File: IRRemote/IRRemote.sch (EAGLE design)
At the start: 18 parts, among them U1 PNA460XM, U3 ATTINY841

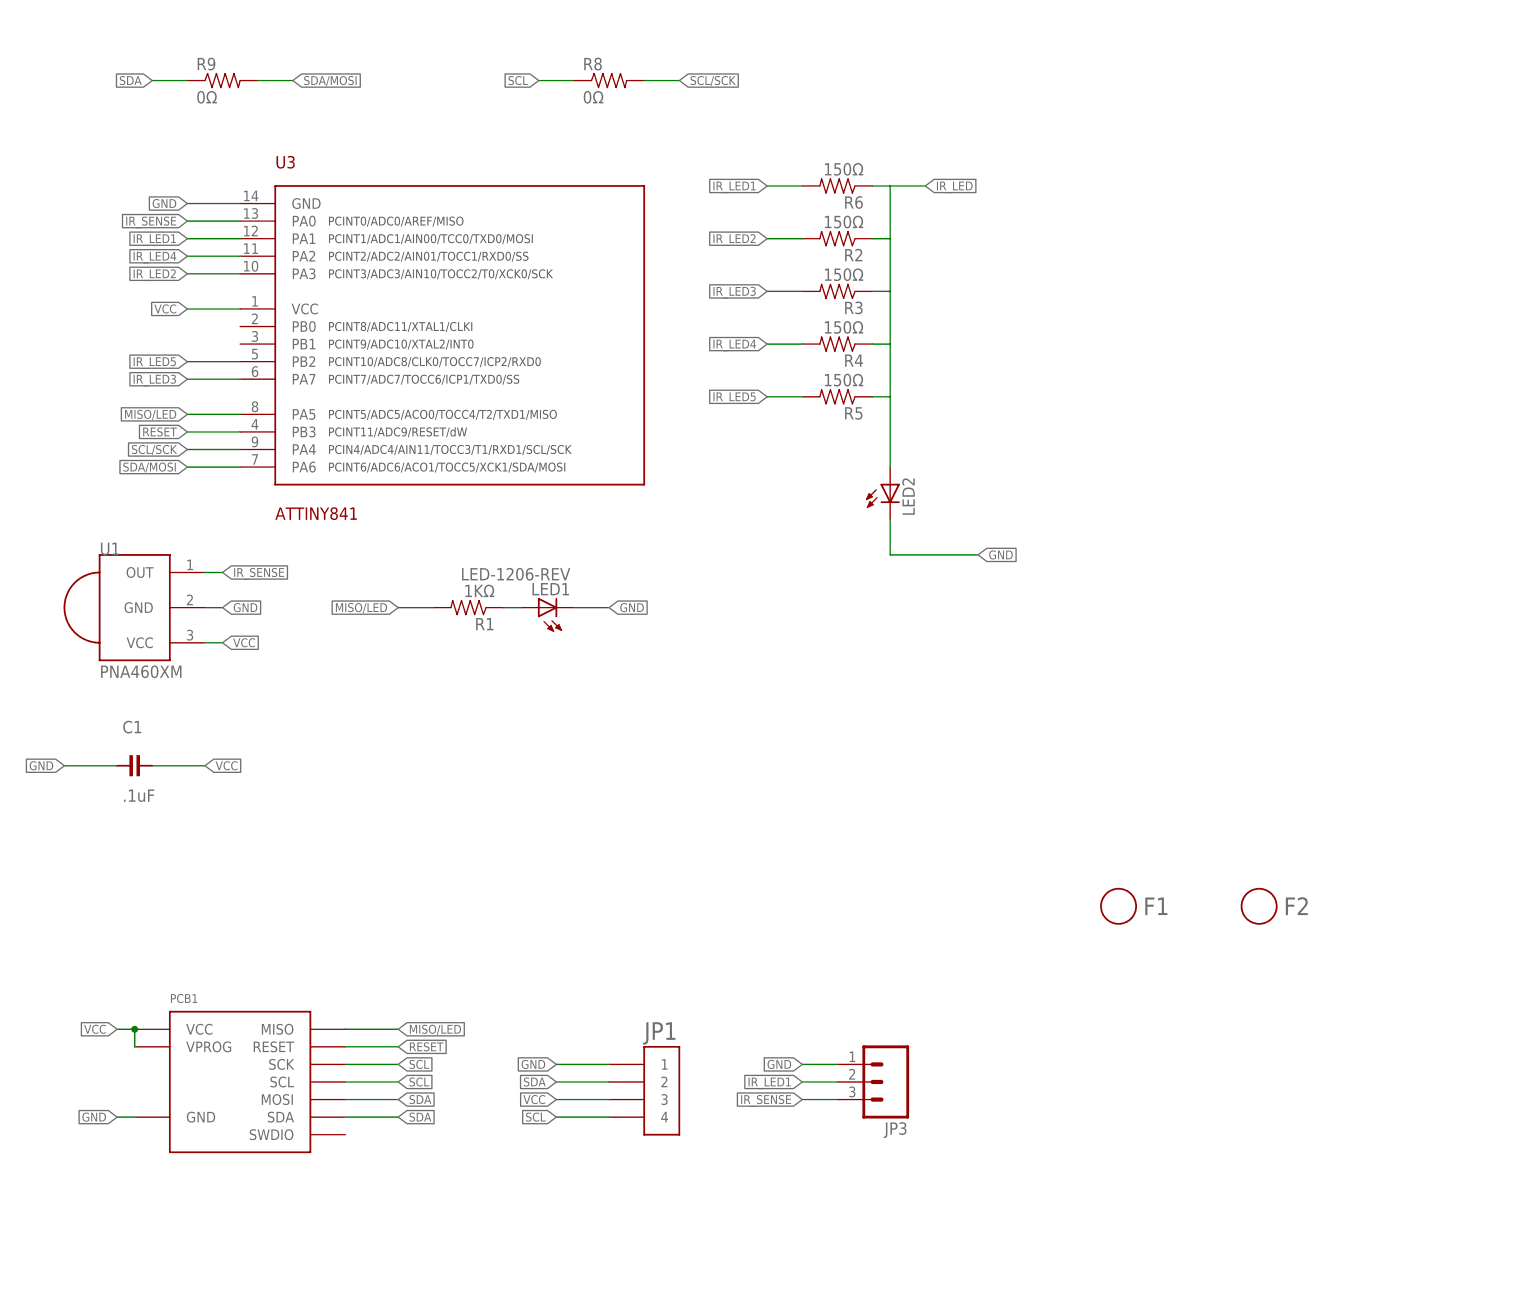
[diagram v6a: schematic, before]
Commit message: Added unique board prefixes to part numbers due to CM requirements
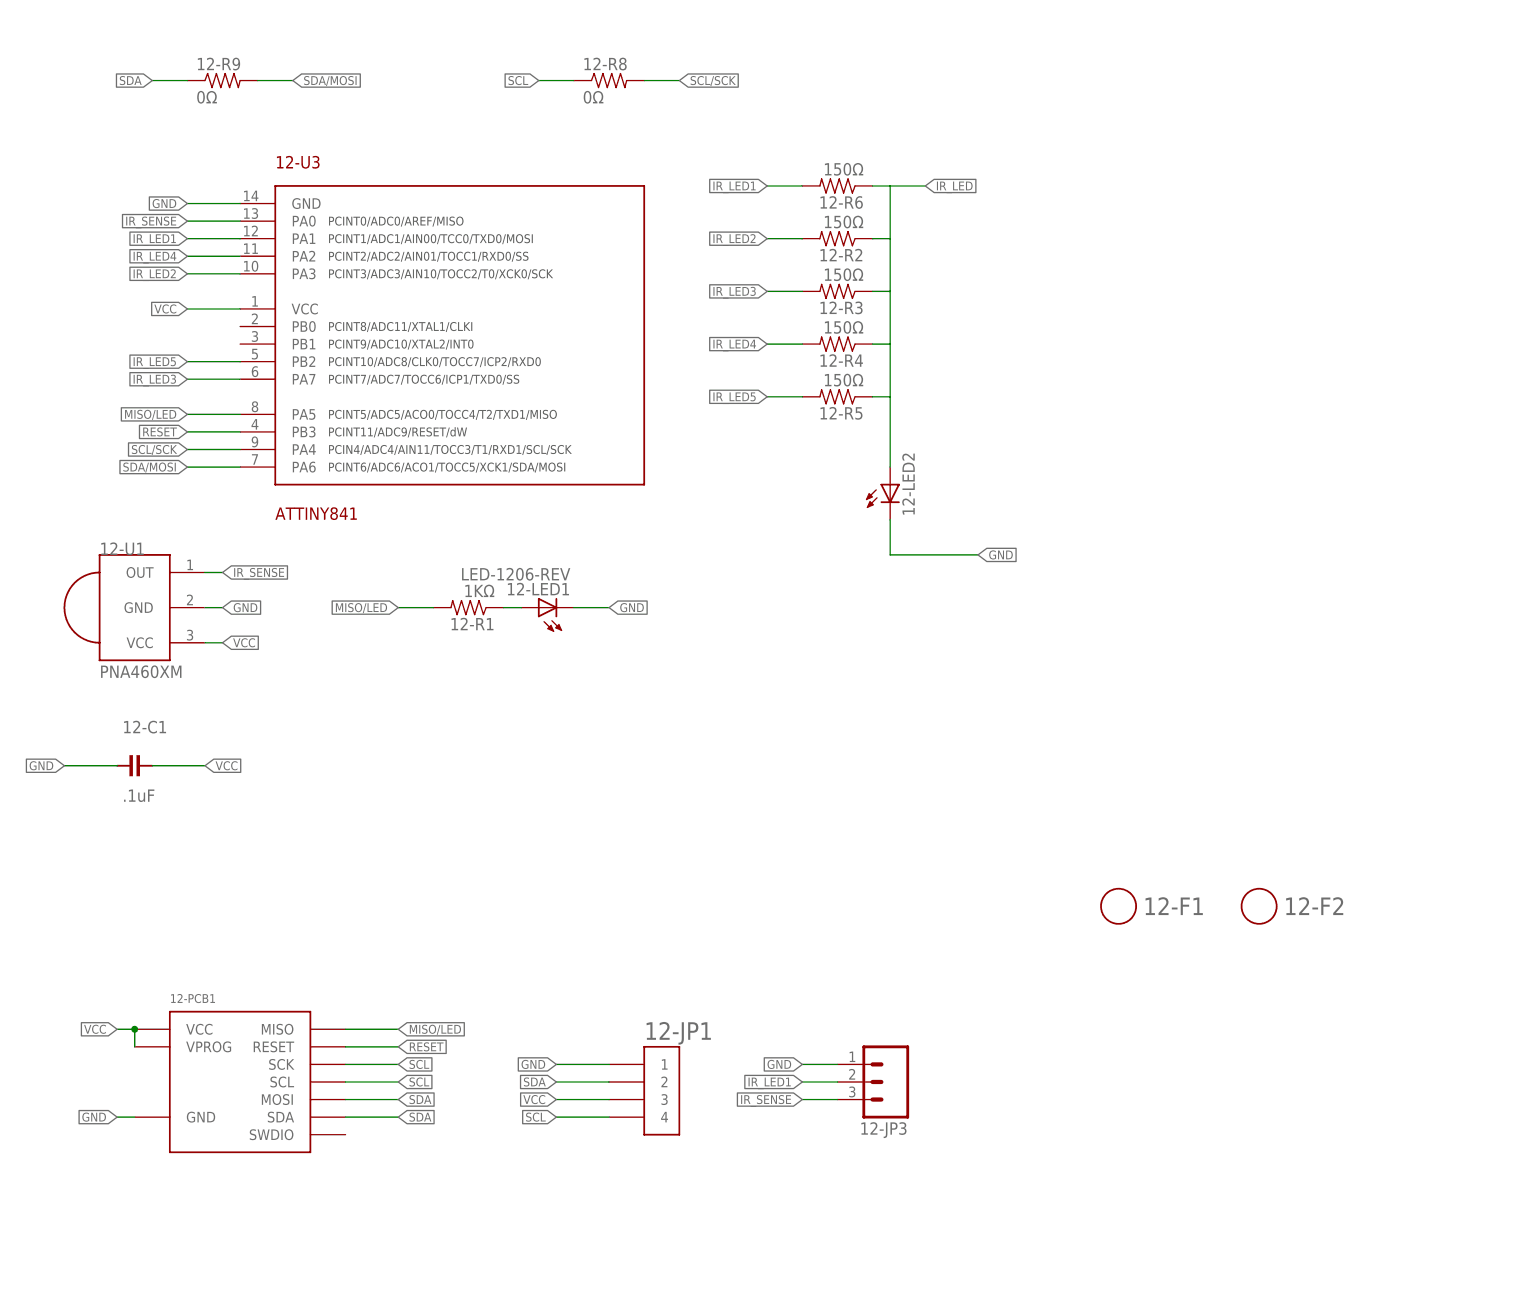
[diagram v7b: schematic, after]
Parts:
- renumbered C1 to 12-C1, F1 to 12-F1, F2 to 12-F2, JP1 to 12-JP1, JP3 to 12-JP3, LED1 to 12-LED1, LED2 to 12-LED2, PCB1 to 12-PCB1, R1 to 12-R1, R2 to 12-R2, R3 to 12-R3, R4 to 12-R4, R5 to 12-R5, R6 to 12-R6, R8 to 12-R8, R9 to 12-R9, U1 to 12-U1, U3 to 12-U3
